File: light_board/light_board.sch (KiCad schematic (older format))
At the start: 17 parts, among them J1 CONN_01X02, J2 Screw_Terminal_1x02, J3 Screw_Terminal_1x02, Q1 FDC658AP, U1 LM3409MY

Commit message: Actually made the changes on the pcb
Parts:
- C2, C3: footprint agg:0805 -> Capacitors_SMD:C_0603
- R1, R2, R3, R4, R5: footprint agg:0805 -> Resistors_SMD:R_0603
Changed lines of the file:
@@
 F 0 "R1" V 4180 3500 50  0000 C CNN
 F 1 "1K" V 4100 3500 50  0000 C CNN
-F 2 "agg:0805" V 4030 3500 50  0001 C CNN
+F 2 "Resistors_SMD:R_0603" V 4030 3500 50  0001 C CNN
 F 3 "" H 4100 3500 50  0001 C CNN
 	1    4100 3500
@@
 F 0 "C2" H 4975 2900 50  0000 L CNN
 F 1 "1uF" H 4975 2700 50  0000 L CNN
-F 2 "agg:0805" H 4988 2650 50  0001 C CNN
+F 2 "Capacitors_SMD:C_0603" H 4988 2650 50  0001 C CNN
 F 3 "" H 4950 2800 50  0001 C CNN
 	1    4950 2800
@@
 F 0 "R4" V 8080 2500 50  0000 C CNN
 F 1 "1K8" V 8000 2500 50  0000 C CNN
-F 2 "agg:0805" V 7930 2500 50  0001 C CNN
+F 2 "Resistors_SMD:R_0603" V 7930 2500 50  0001 C CNN
 F 3 "" H 8000 2500 50  0001 C CNN
 	1    8000 2500
@@
 F 0 "R5" V 8330 2750 50  0000 C CNN
 F 1 "15K" V 8250 2750 50  0000 C CNN
-F 2 "agg:0805" V 8180 2750 50  0001 C CNN
+F 2 "Resistors_SMD:R_0603" V 8180 2750 50  0001 C CNN
 F 3 "" H 8250 2750 50  0001 C CNN
 	1    8250 2750
@@
 F 0 "C3" H 7575 4800 50  0000 L CNN
 F 1 "1nF" H 7575 4600 50  0000 L CNN
-F 2 "agg:0805" H 7588 4550 50  0001 C CNN
+F 2 "Capacitors_SMD:C_0603" H 7588 4550 50  0001 C CNN
 F 3 "" H 7550 4700 50  0001 C CNN
 	1    7550 4700
@@
 F 0 "R3" V 7980 4450 50  0000 C CNN
 F 1 "3K9" V 7900 4450 50  0000 C CNN
-F 2 "agg:0805" V 7830 4450 50  0001 C CNN
+F 2 "Resistors_SMD:R_0603" V 7830 4450 50  0001 C CNN
 F 3 "" H 7900 4450 50  0001 C CNN
 	1    7900 4450
@@
 F 0 "R2" V 4480 3900 50  0000 C CNN
 F 1 "4.7K" V 4400 3900 50  0000 C CNN
-F 2 "agg:0805" V 4330 3900 50  0001 C CNN
+F 2 "Resistors_SMD:R_0603" V 4330 3900 50  0001 C CNN
 F 3 "" H 4400 3900 50  0001 C CNN
 	1    4400 3900

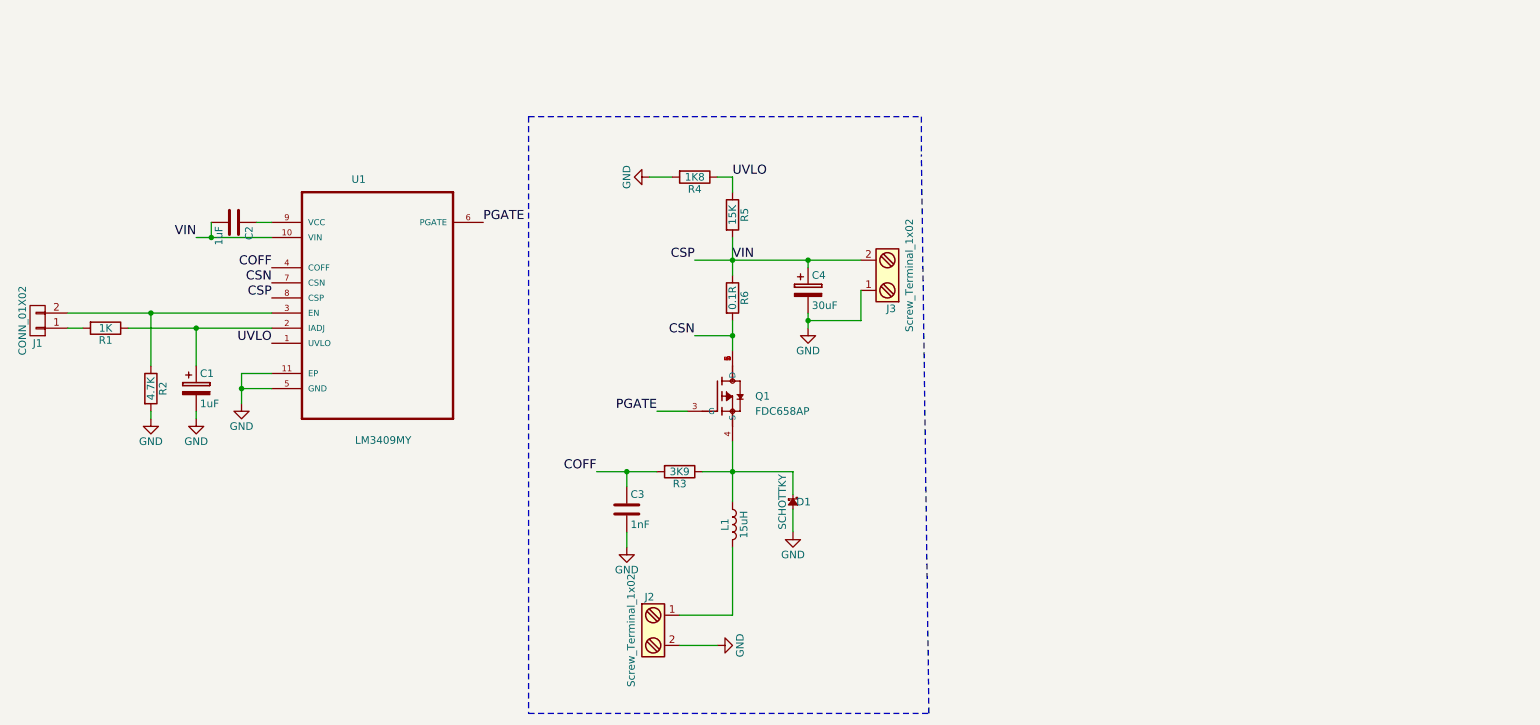
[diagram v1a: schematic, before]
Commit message: Added comments to light board
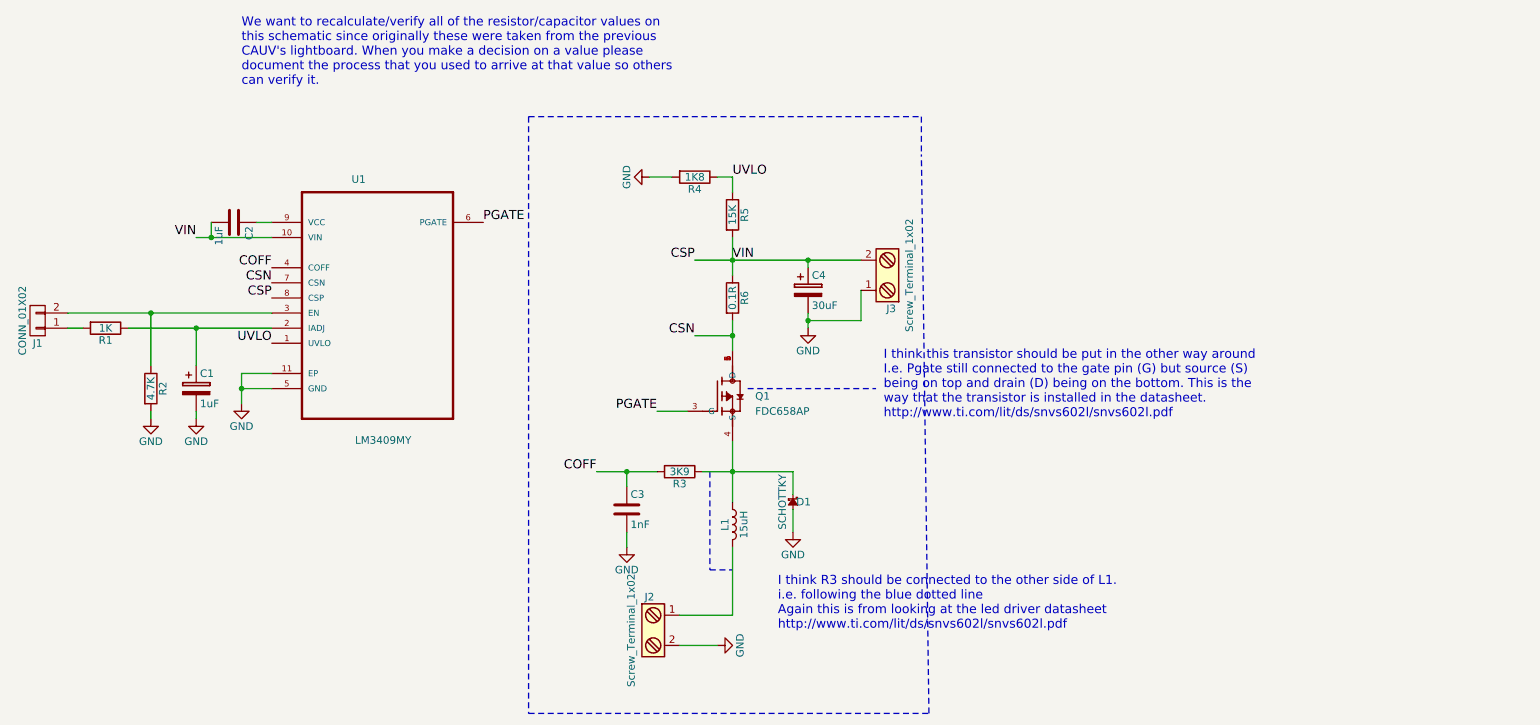
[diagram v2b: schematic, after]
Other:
- note added: "I think R3 should be connected to the other side of L1.\ni.e. following the blue dotted line\nAgain this is from looking at the led driver datasheet\nhttp://www.ti.com/lit/ds/snvs602l/snvs602l.pdf"
- note added: "I think this transistor should be put in the other way around\nI.e. Pgate still connected to the gate pin (G) but source (S) \nbeing on top and drain (D) being on the bottom. This is the\nway that the transistor is installed in the datasheet. \nhttp://www.ti.com/lit/ds/snvs602l/snvs602l.pdf"
- note added: "We want to recalculate/verify all of the resistor/capacitor values on\nthis schematic since originally these were taken from the previous\nCAUV's lightboard. When you make a decision on a value please\ndocument the process that you used to arrive at that value so others\ncan verify it."
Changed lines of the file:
@@
 	0    1    1    0
 $EndComp
-Wire Wire Line
-	5200 3800 5000 3800
-Wire Wire Line
-	5000 3800 5000 4000
-Wire Wire Line
-	5200 3900 5000 3900
-Connection ~ 5000 3900
-Wire Wire Line
-	5200 3500 4250 3500
-Wire Wire Line
-	4700 3750 4700 3500
-Connection ~ 4700 3500
-Wire Wire Line
-	4400 3750 4400 3400
-Wire Wire Line
-	3850 3400 5200 3400
-Wire Wire Line
-	3850 3500 3950 3500
-Connection ~ 4400 3400
-Wire Wire Line
-	5100 2800 5200 2800
-Wire Wire Line
-	4700 2900 5200 2900
-Wire Wire Line
-	4800 2800 4800 2900
-Connection ~ 4800 2900
 Text Label 5200 3100 2    60   ~ 0
 COFF
@@
 Text Label 8250 3050 0    60   ~ 0
 VIN
-Wire Wire Line
-	7700 2500 7850 2500
-Wire Wire Line
-	8250 2900 8250 3150
-Wire Wire Line
-	8150 2500 8250 2500
-Wire Wire Line
-	8250 2500 8250 2600
 Text Label 7350 4450 2    60   ~ 0
 COFF
@@
 	1    0    0    -1
 $EndComp
-Wire Wire Line
-	8050 4450 8650 4450
-Wire Wire Line
-	8250 4250 8250 4650
-Connection ~ 8250 4450
-Wire Wire Line
-	8650 4700 8650 4850
-Wire Wire Line
-	8650 4450 8650 4600
-Wire Wire Line
-	7350 4450 7750 4450
 $Comp
 L GND #PWR06
@@
 	1    0    0    -1
 $EndComp
-Wire Wire Line
-	7550 4950 7550 4850
-Wire Wire Line
-	7550 4450 7550 4550
-Connection ~ 7550 4450
-Wire Wire Line
-	8250 4950 8250 5400
 $Comp
 L R R6
@@
 	1    0    0    -1
 $EndComp
-Wire Wire Line
-	8250 3650 8250 3450
-Wire Wire Line
-	8000 3550 8250 3550
-Connection ~ 8250 3550
 $Comp
 L CP C4
@@
 	1    0    0    -1
 $EndComp
-Connection ~ 8250 3050
-Wire Wire Line
-	8000 3050 9100 3050
 $Comp
 L CP C1
@@
 	1    0    0    -1
 $EndComp
-Wire Wire Line
-	8250 5400 7900 5400
 $Comp
 L R R2
@@
 	1    0    0    -1
 $EndComp
-Wire Wire Line
-	4400 4050 4400 4100
-Wire Wire Line
-	4700 4100 4700 4050
 $Comp
 L GND #PWR08
@@
 	0    -1   -1   0
 $EndComp
-Wire Wire Line
-	7900 5600 8150 5600
 $Comp
 L FDC658AP Q1
@@
 	1    0    0    -1
 $EndComp
-Wire Wire Line
-	7950 4050 7750 4050
-Wire Wire Line
-	8750 3500 8750 3400
-Wire Notes Line
-	6900 2100 6900 6050
-Wire Notes Line
-	6900 6050 9550 6050
-Wire Notes Line
-	9550 6050 9500 2350
-Wire Notes Line
-	6900 2100 9500 2100
-Wire Notes Line
-	9500 2100 9500 2350
-Wire Wire Line
-	8750 3050 8750 3100
 $Comp
 L Screw_Terminal_1x02 J3
@@
 	-1   0    0    1
 $EndComp
+Text Notes 9250 4100 0    60   ~ 0
+I think this transistor should be put in the other way around\nI.e. Pgate still connected to the gate pin (G) but source (S) \nbeing on top and drain (D) being on the bottom. This is the\nway that the transistor is installed in the datasheet. \nhttp://www.ti.com/lit/ds/snvs602l/snvs602l.pdf
+Wire Wire Line
+	5200 3800 5000 3800
+Wire Wire Line
+	5000 3800 5000 4000
+Wire Wire Line
+	5200 3900 5000 3900
+Connection ~ 5000 3900
+Wire Wire Line
+	5200 3500 4250 3500
+Wire Wire Line
+	4700 3750 4700 3500
+Connection ~ 4700 3500
+Wire Wire Line
+	4400 3750 4400 3400
+Wire Wire Line
+	3850 3400 5200 3400
+Wire Wire Line
+	3850 3500 3950 3500
+Connection ~ 4400 3400
+Wire Wire Line
+	5100 2800 5200 2800
+Wire Wire Line
+	4700 2900 5200 2900
+Wire Wire Line
+	4800 2800 4800 2900
+Connection ~ 4800 2900
+Wire Wire Line
+	7700 2500 7850 2500
+Wire Wire Line
+	8250 2900 8250 3150
+Wire Wire Line
+	8150 2500 8250 2500
+Wire Wire Line
+	8250 2500 8250 2600
+Wire Wire Line
+	8050 4450 8650 4450
+Wire Wire Line
+	8250 4250 8250 4650
+Connection ~ 8250 4450
+Wire Wire Line
+	8650 4700 8650 4850
+Wire Wire Line
+	8650 4450 8650 4600
+Wire Wire Line
+	7350 4450 7750 4450
+Wire Wire Line
+	7550 4950 7550 4850
+Wire Wire Line
+	7550 4450 7550 4550
+Connection ~ 7550 4450
+Wire Wire Line
+	8250 4950 8250 5400
+Wire Wire Line
+	8250 3650 8250 3450
+Wire Wire Line
+	8000 3550 8250 3550
+Connection ~ 8250 3550
+Connection ~ 8250 3050
+Wire Wire Line
+	8000 3050 9100 3050
+Wire Wire Line
+	8250 5400 7900 5400
+Wire Wire Line
+	4400 4050 4400 4100
+Wire Wire Line
+	4700 4100 4700 4050
+Wire Wire Line
+	7900 5600 8150 5600
+Wire Wire Line
+	7950 4050 7750 4050
+Wire Wire Line
+	8750 3500 8750 3400
+Wire Notes Line
+	6900 2100 6900 6050
+Wire Notes Line
+	6900 6050 9550 6050
+Wire Notes Line
+	9550 6050 9500 2350
+Wire Notes Line
+	6900 2100 9500 2100
+Wire Notes Line
+	9500 2100 9500 2350
+Wire Wire Line
+	8750 3050 8750 3100
 Connection ~ 8750 3050
 Wire Wire Line
@@
 	9100 3450 8750 3450
 Connection ~ 8750 3450
+Wire Notes Line
+	8350 3900 9200 3900
+Text Notes 8550 5500 0    60   ~ 0
+I think R3 should be connected to the other side of L1.\ni.e. following the blue dotted line\nAgain this is from looking at the led driver datasheet\nhttp://www.ti.com/lit/ds/snvs602l/snvs602l.pdf
+Wire Notes Line
+	8100 4450 8100 5100
+Wire Notes Line
+	8100 5100 8250 5100
+Text Notes 5000 1900 0    60   ~ 0
+We want to recalculate/verify all of the resistor/capacitor values on\nthis schematic since originally these were taken from the previous\nCAUV's lightboard. When you make a decision on a value please\ndocument the process that you used to arrive at that value so others\ncan verify it.
 $EndSCHEMATC

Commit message: added mounting holes and changed light board footprints
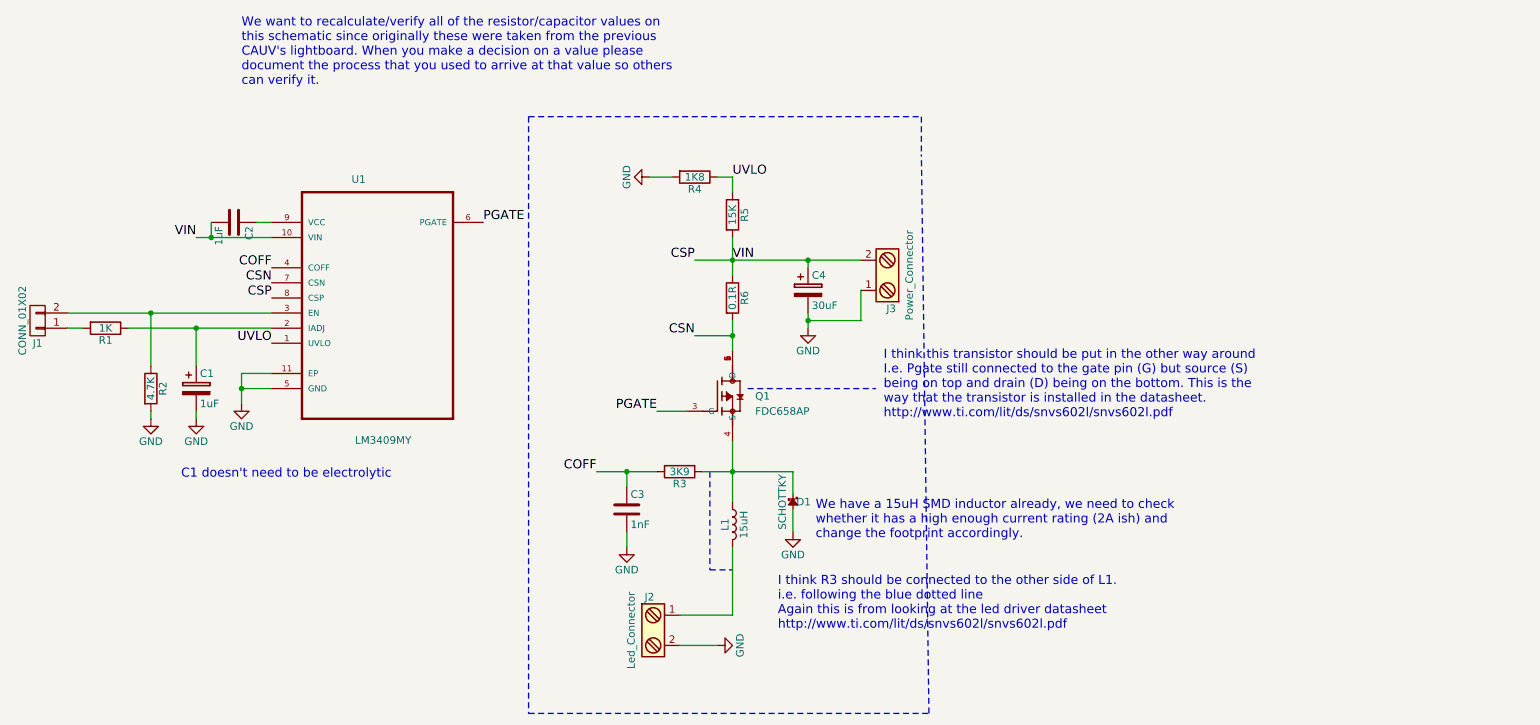
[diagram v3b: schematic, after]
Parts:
- J2: value Screw_Terminal_1x02 -> Led_Connector; footprint footprints:POWER_CONN -> Connectors_Terminal_Blocks:TerminalBlock_Philmore_TB132_02x5mm_Straight
- J3: value Screw_Terminal_1x02 -> Power_Connector; footprint footprints:POWER_CONN -> Connectors_Terminal_Blocks:TerminalBlock_Pheonix_MPT-2.54mm_2pol
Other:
- note added: "C1 doesn't need to be electrolytic"
- note added: "We have a 15uH SMD inductor already, we need to check\nwhether it has a high enough current rating (2A ish) and \nchange the footprint accordingly."
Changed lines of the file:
@@
 P 7700 5500
 F 0 "J2" H 7700 5750 50  0000 C TNN
-F 1 "Screw_Terminal_1x02" V 7550 5500 50  0000 C TNN
-F 2 "footprints:POWER_CONN" H 7700 5275 50  0001 C CNN
+F 1 "Led_Connector" V 7550 5500 50  0000 C TNN
+F 2 "Connectors_Terminal_Blocks:TerminalBlock_Philmore_TB132_02x5mm_Straight" H 7700 5275 50  0001 C CNN
 F 3 "" H 7675 5500 50  0001 C CNN
 	1    7700 5500
@@
 P 9300 3150
 F 0 "J3" H 9300 3400 50  0000 C TNN
-F 1 "Screw_Terminal_1x02" V 9150 3150 50  0000 C TNN
-F 2 "footprints:POWER_CONN" H 9300 2925 50  0001 C CNN
+F 1 "Power_Connector" V 9150 3150 50  0000 C TNN
+F 2 "Connectors_Terminal_Blocks:TerminalBlock_Pheonix_MPT-2.54mm_2pol" H 9300 2925 50  0001 C CNN
 F 3 "" H 9275 3150 50  0001 C CNN
 	1    9300 3150
@@
 Text Notes 5000 1900 0    60   ~ 0
 We want to recalculate/verify all of the resistor/capacitor values on\nthis schematic since originally these were taken from the previous\nCAUV's lightboard. When you make a decision on a value please\ndocument the process that you used to arrive at that value so others\ncan verify it.
+Text Notes 8800 4900 0    60   ~ 0
+We have a 15uH SMD inductor already, we need to check\nwhether it has a high enough current rating (2A ish) and \nchange the footprint accordingly.
+Text Notes 4600 4500 0    60   ~ 0
+C1 doesn't need to be electrolytic
 $EndSCHEMATC
